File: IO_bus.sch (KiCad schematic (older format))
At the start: 3 parts

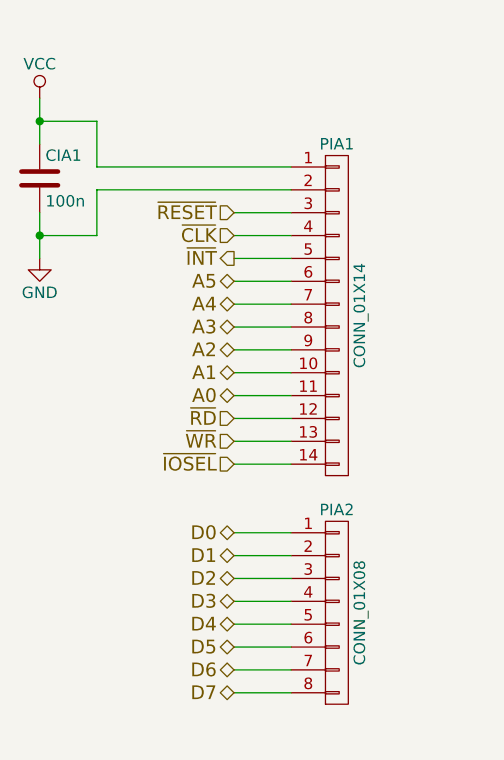
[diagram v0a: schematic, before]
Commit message: Update with smaller board and through-hole parts.
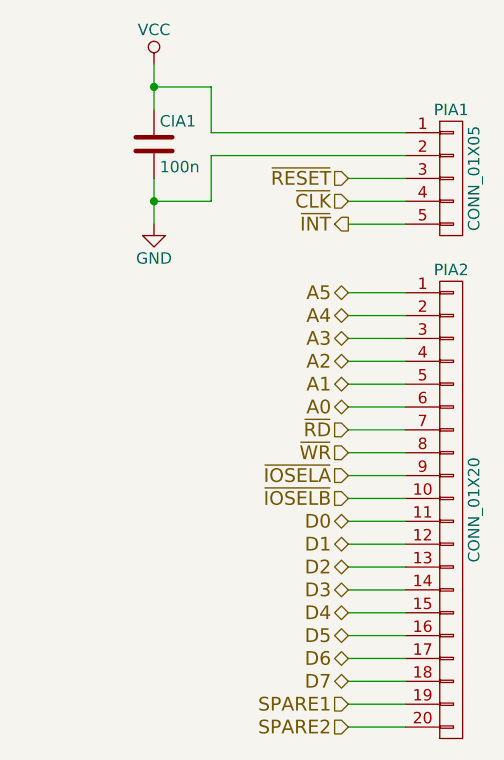
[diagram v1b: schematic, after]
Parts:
- removed PIA1: CONN_01X14, Socket_Strips:Socket_Strip_Straight_1x14, symbol CONN_01X14
- removed PIA2: CONN_01X08, Socket_Strips:Socket_Strip_Straight_1x08, symbol CONN_01X08
- added PIA1: CONN_01X05, Socket_Strips:Socket_Strip_Straight_1x05, symbol CONN_01X05
- added PIA2: CONN_01X20, Socket_Strips:Socket_Strip_Straight_1x20, symbol CONN_01X20
- CIA1: footprint Capacitors_SMD:C_0805_HandSoldering -> Capacitors_ThroughHole:C_Rect_L4_W2.5_P2.5
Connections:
- net A0: now also PIA2.6 (P6)
- net A1: now also PIA2.5 (P5)
- net A2: now also PIA2.4 (P4)
- net A3: now also PIA2.3 (P3)
- net A4: now also PIA2.2 (P2)
- net A5: now also PIA2.1 (P1)
- net D0: now also PIA2.11 (P11)
- net D1: now also PIA2.12 (P12)
- net D2: now also PIA2.13 (P13)
- net D3: now also PIA2.14 (P14)
- net D4: now also PIA2.15 (P15)
- net D5: now also PIA2.16 (P16)
- net D6: now also PIA2.17 (P17)
- net D7: now also PIA2.18 (P18)
- net GND: now also PIA1.2 (P2)
- net VCC: now also PIA1.1 (P1)
- net ~CLK: now also PIA1.4 (P4)
- net ~INT: now also PIA1.5 (P5)
- net ~RD: now also PIA2.7 (P7)
- net ~RESET: now also PIA1.3 (P3)
- net ~WR: now also PIA2.8 (P8)
- new net SPARE1: PIA2.19 (P19)
- new net SPARE2: PIA2.20 (P20)
- new net ~IOSELA: PIA2.9 (P9)
- new net ~IOSELB: PIA2.10 (P10)
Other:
- moved on the sheet: CIA1
